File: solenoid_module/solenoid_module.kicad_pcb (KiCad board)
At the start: 2 copper layers, 16 parts, among them J1 1x5 2.54, J2 1x5 2.54, J3 1x2 5.08, J4 1x2 5.08, J5 1x3 5.08, Q1 BC817, SW1 3way switch, U1 TMCS1107A3, U2 ADS1115IDGS

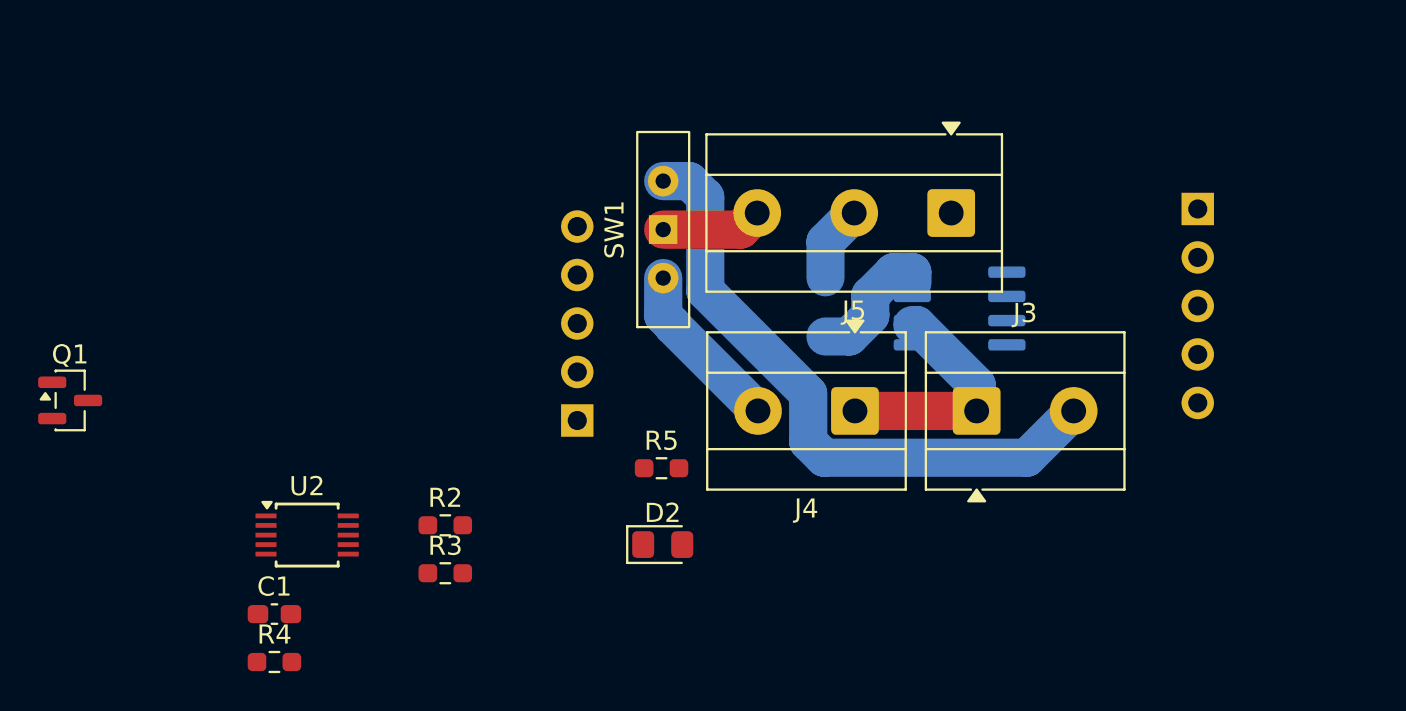
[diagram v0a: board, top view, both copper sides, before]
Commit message: Solenoid module v1.0.0
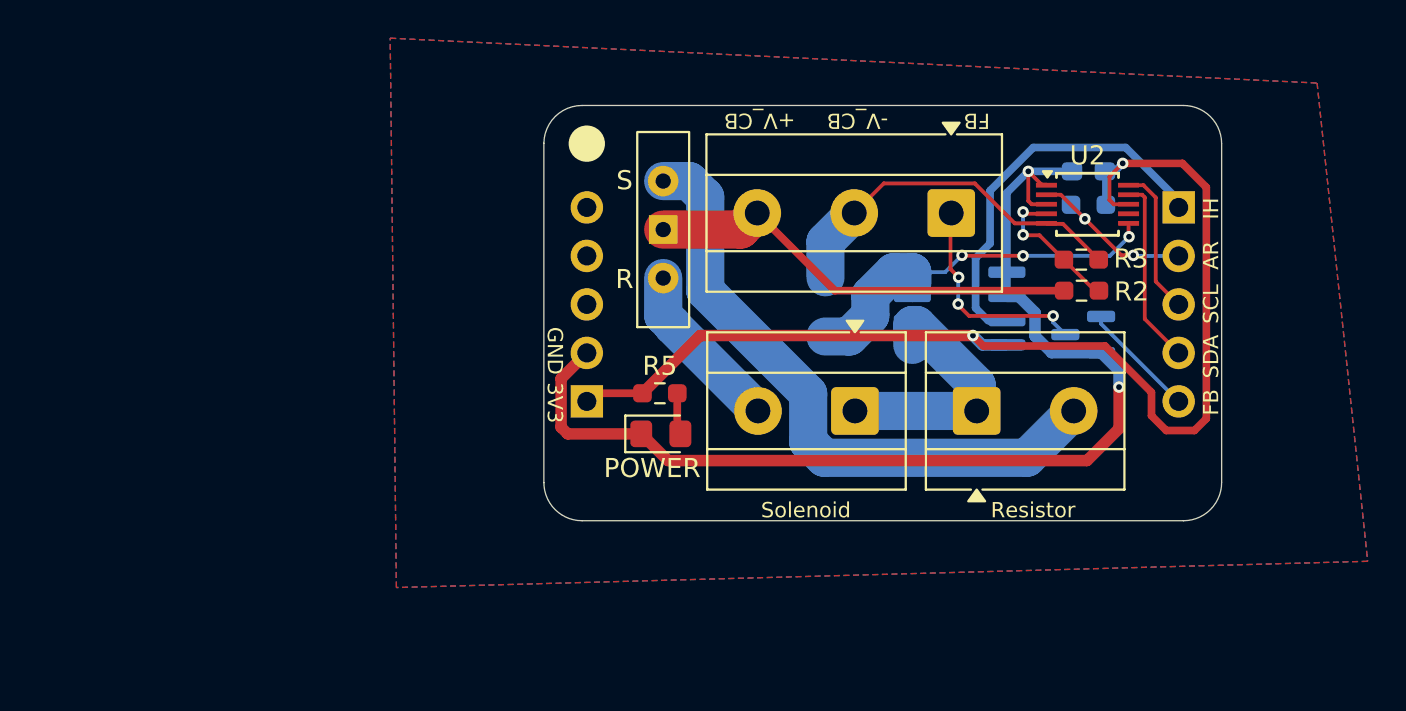
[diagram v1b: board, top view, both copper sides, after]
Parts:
- added G***: LOGO, LOGO, B.Cu at (60.6, 45.4)
- C1, Q1, R4: moved to B.Cu
- moved Q1 53.2 mm to (82.0, 36.5), turned to 180 degrees
- moved R4 48.9 mm to (82.3, 29.7)
- moved C1 48.5 mm to (82.3, 27.9), turned to 180 degrees
- moved U2 44.4 mm to (82.2, 29.7)
- moved R3 37.1 mm to (81.9, 32.6)
- moved R2 35.5 mm to (81.9, 34.2)
- moved POWER 5.80 mm to (59.9, 41.7)
- moved R5 3.93 mm to (59.8, 39.6)
- moved J1 1.12 mm to (56.0, 40.0)
- moved J2 1.00 mm to (87.0, 29.8)
- renumbered D2 to POWER, J3 to Resistor, J4 to Solenoid
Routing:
- net +3V3: track 0.00 -> 62.2 mm, vias 0 -> 2
- net GND: track 0.00 -> 59.5 mm, vias 0 -> 2
- net /Current measure/I_Hall: track 0.00 -> 20.7 mm
- net +12V_camera_box: track 5.28 -> 23.0 mm
- net /ADC/A1: track 3.99 -> 19.1 mm
- net /ADC/A2: track 7.13 -> 20.0 mm, vias 0 -> 3
- net Net-(J5-Pin_1): track 0.00 -> 11.5 mm, vias 0 -> 3
- net SDA: track 0.00 -> 9.79 mm
- net /ADC/ALERT/READY: track 0.00 -> 9.29 mm, vias 0 -> 2
- net SCL: track 0.00 -> 7.79 mm
- net /ADC/A0: track 0.00 -> 7.65 mm, vias 0 -> 2
- net Net-(J2-Pin_5): track 0.00 -> 6.13 mm
- net Net-(D2-A): track 0.00 -> 2.19 mm
- net /Current measure/IN+: track 12.4 -> 13.4 mm
- added copper zone on B.Cu, net (none)
- added copper zone on F.Cu, net (none)
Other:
- board outline added: 35.5 x 21.8 mm
- board text added: "+V_CB"
- board text added: "-V_CB"
- board text added: "3V3"
- board text added: "AR"
- board text added: "FB"
- board text added: "GND"
- board text added: "IH"
- board text added: "R"
- board text added: "S"
- board text added: "SCL"
- board text added: "SDA"
- board text added: "solenoid module v1.0.0"

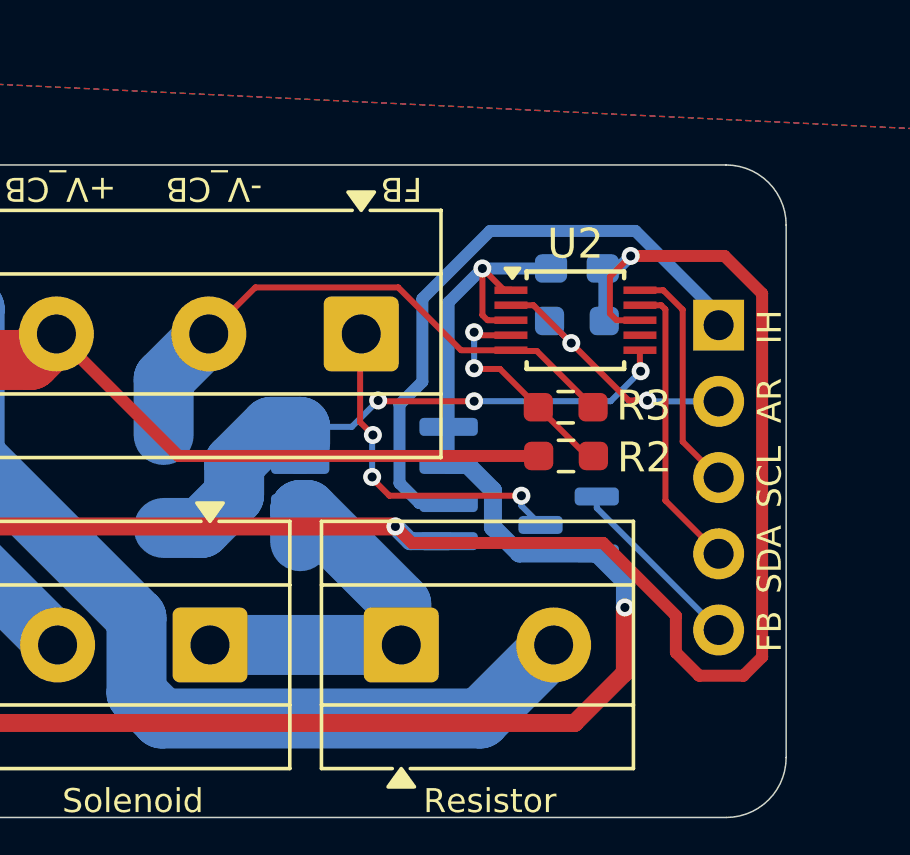
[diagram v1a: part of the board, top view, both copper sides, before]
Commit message: solenoid_main_board schematic
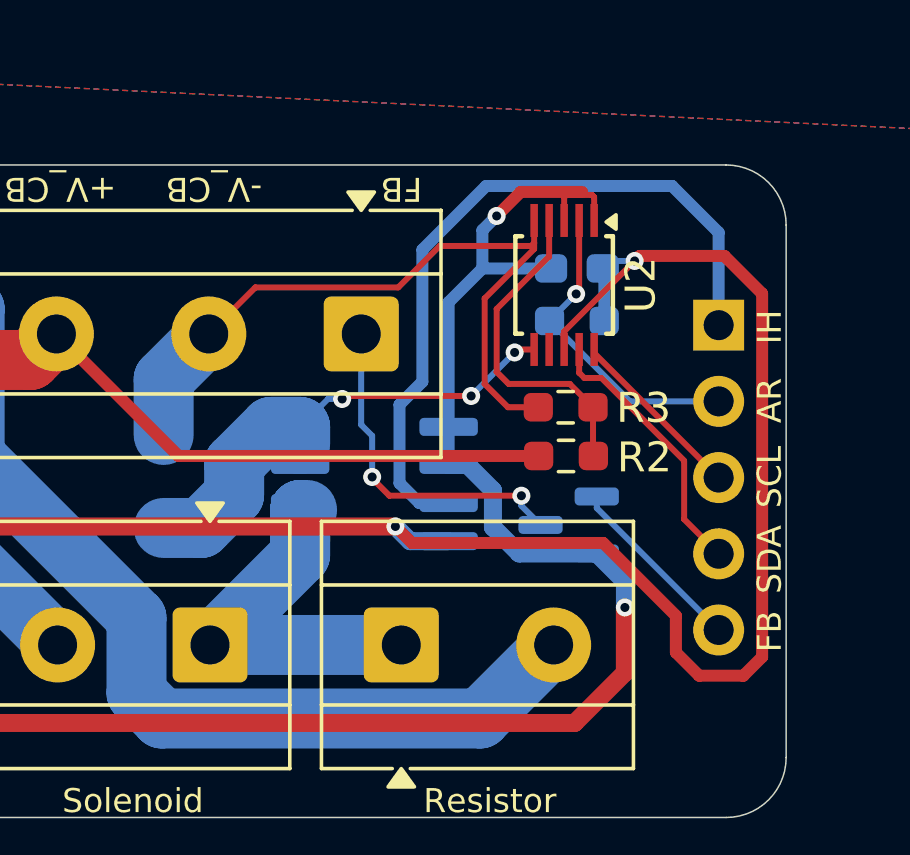
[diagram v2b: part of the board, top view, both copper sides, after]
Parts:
- moved U2 1.23 mm to (81.8, 28.5), turned to -90 degrees
- turned R3 to 180 degrees
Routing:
- net /ADC/A1: track 19.1 -> 24.3 mm
- net /ADC/A2: track 20.0 -> 16.0 mm
- net GND: track 59.5 -> 63.4 mm
- net /Current measure/I_Hall: track 20.7 -> 24.5 mm
- net /ADC/A0: track 7.65 -> 11.4 mm, vias 2 -> 0
- net SCL: track 7.79 -> 5.99 mm
- net /ADC/ALERT/READY: track 9.29 -> 10.5 mm, vias 2 -> 1
- net SDA: track 9.79 -> 9.07 mm
- net +3V3: track 62.2 -> 62.8 mm
- net Net-(J5-Pin_1): vias 3 -> 2
